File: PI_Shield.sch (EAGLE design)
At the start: 64 parts, among them J10 T2I, J11 T2I, J12 T2I, J13 DF13-4P-1.25DSA, J14 DF13-4P-1.25DSA, J15 DF13-4P-1.25DSA, J16 T2I5P, Q1 220mA/50V/3.5Ω, Q3 220mA/50V/3.5Ω, Q4 220mA/50V/3.5Ω, Q5 2.5A/30V/105mΩ, U1 MAX1136EUA-T, U2 AZ1117EH-3.3TRG1, Y1 ECS-80-S-4X

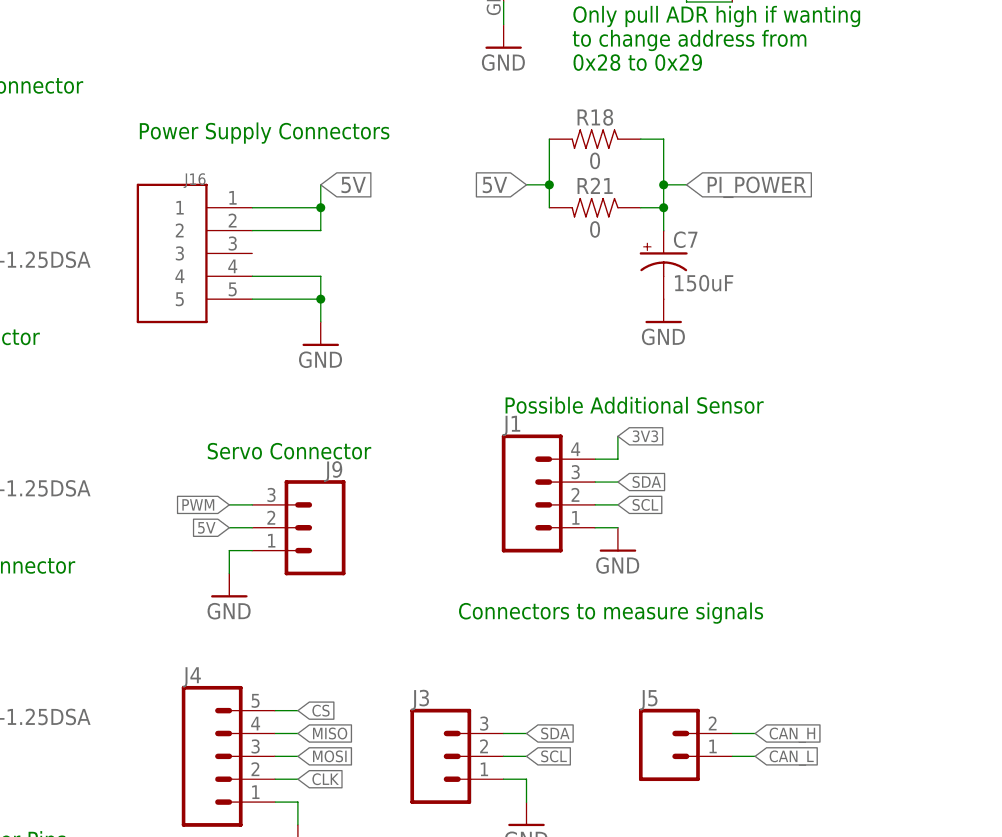
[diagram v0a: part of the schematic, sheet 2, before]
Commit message: add micro usb connector for external powering while testing
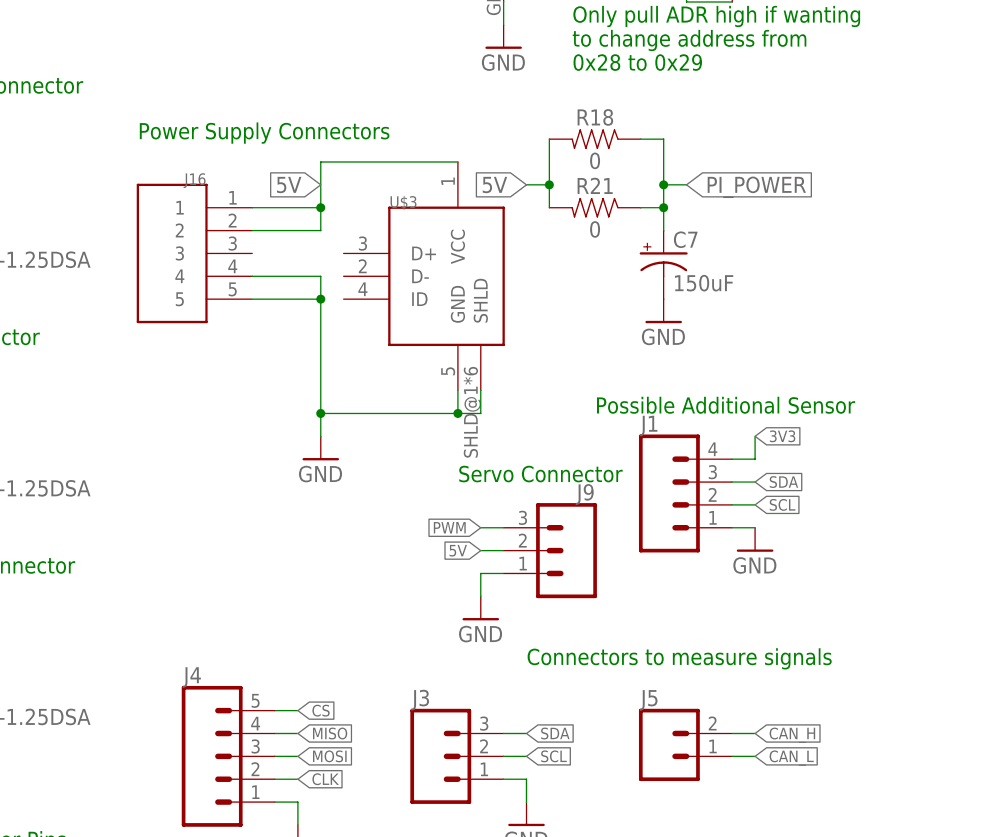
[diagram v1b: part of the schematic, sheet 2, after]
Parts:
- added U$3: USB-MICRO, usb conn:USB-MICRO
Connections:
- net 5V: now also U$3.VCC
- net GND: now also U$3.GND, U$3.SHLD
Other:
- moved on the sheet: J1, J9
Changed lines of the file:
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@@
 <part name="U$5" library="Adafruit IMUs - BNO055 and FX" deviceset="ADAFRUIT-BNO055" device=""/>
 <part name="GND31" library="supply1" library_urn="urn:adsk.eagle:library:371" deviceset="GND" device=""/>
+<part name="U$3" library="usb conn" deviceset="USB-MICRO" device=""/>
 </parts>
 <sheets>
@@
 <sheet>
 <plain>
-<text x="210.82" y="53.34" size="1.778" layer="91">Connectors to measure signals</text>
+<text x="218.44" y="48.26" size="1.778" layer="91">Connectors to measure signals</text>
 <text x="134.62" y="111.76" size="1.778" layer="91">Temperature Sensor Connector</text>
 <text x="134.62" y="83.82" size="1.778" layer="91">Pressure Sensor Connector</text>
@@
 <text x="193.04" y="160.02" size="1.778" layer="91">BNO055 IMU</text>
 <text x="175.26" y="106.68" size="1.778" layer="91">Power Supply Connectors</text>
-<text x="215.9" y="76.2" size="1.778" layer="91">Possible Additional Sensor</text>
+<text x="226.06" y="76.2" size="1.778" layer="91">Possible Additional Sensor</text>
 <text x="129.54" y="27.94" size="1.778" layer="91">UART Communication Header Pins</text>
-<text x="182.88" y="71.12" size="1.778" layer="91">Servo Connector</text>
+<text x="210.82" y="68.58" size="1.778" layer="91">Servo Connector</text>
 <text x="76.2" y="63.5" size="1.778" layer="91" rot="R90">We will be using Pi 4, not Pi 2</text>
 <text x="50.8" y="121.92" size="1.778" layer="91" rot="R180">DO NOT use pin 28 or 27
@@
 <attribute name="NAME" x="231.14" y="43.688" size="1.778" layer="95" font="vector"/>
 </instance>
-<instance part="GND3" gate="1" x="195.58" y="83.82" smashed="yes">
-<attribute name="VALUE" x="193.04" y="81.28" size="1.778" layer="96"/>
+<instance part="GND3" gate="1" x="195.58" y="71.12" smashed="yes">
+<attribute name="VALUE" x="193.04" y="68.58" size="1.778" layer="96"/>
 </instance>
 <instance part="C13" gate="G$1" x="238.76" y="152.4" smashed="yes">
@@
 <attribute name="VALUE" x="240.284" y="150.241" size="1.778" layer="96" font="vector"/>
 </instance>
-<instance part="J1" gate="G$1" x="220.98" y="66.04" smashed="yes">
-<attribute name="VALUE" x="215.9" y="58.674" size="1.778" layer="96" font="vector"/>
-<attribute name="NAME" x="215.9" y="74.168" size="1.778" layer="95" font="vector"/>
+<instance part="J1" gate="G$1" x="236.22" y="66.04" smashed="yes">
+<attribute name="VALUE" x="231.14" y="58.674" size="1.778" layer="96" font="vector"/>
+<attribute name="NAME" x="231.14" y="74.168" size="1.778" layer="95" font="vector"/>
 </instance>
 <instance part="J8" gate="J$1" x="134.62" y="17.78" smashed="yes">
@@
 <attribute name="VALUE" x="215.9" y="27.94" size="1.778" layer="96"/>
 </instance>
-<instance part="GND26" gate="1" x="228.6" y="60.96" smashed="yes">
-<attribute name="VALUE" x="226.06" y="58.42" size="1.778" layer="96"/>
+<instance part="GND26" gate="1" x="243.84" y="60.96" smashed="yes">
+<attribute name="VALUE" x="241.3" y="58.42" size="1.778" layer="96"/>
 </instance>
 <instance part="GND27" gate="1" x="215.9" y="116.84" smashed="yes">
@@
 <attribute name="VALUE" x="142.24" y="7.62" size="1.778" layer="96"/>
 </instance>
-<instance part="GND23" gate="1" x="185.42" y="55.88" smashed="yes">
-<attribute name="VALUE" x="182.88" y="53.34" size="1.778" layer="96"/>
+<instance part="GND23" gate="1" x="213.36" y="53.34" smashed="yes">
+<attribute name="VALUE" x="210.82" y="50.8" size="1.778" layer="96"/>
 </instance>
 <instance part="R18" gate="G$1" x="226.06" y="106.68" smashed="yes" rot="MR0">
@@
 <attribute name="NAME" x="182.88" y="101.6" size="1.27" layer="95" rot="MR0"/>
 </instance>
-<instance part="J9" gate="J$1" x="195.58" y="63.5" smashed="yes" rot="MR0">
-<attribute name="VALUE" x="198.12" y="56.134" size="1.778" layer="96" font="vector" rot="MR0"/>
-<attribute name="NAME" x="198.12" y="69.088" size="1.778" layer="95" font="vector" rot="MR0"/>
+<instance part="J9" gate="J$1" x="223.52" y="60.96" smashed="yes" rot="MR0">
+<attribute name="VALUE" x="226.06" y="53.594" size="1.778" layer="96" font="vector" rot="MR0"/>
+<attribute name="NAME" x="226.06" y="66.548" size="1.778" layer="95" font="vector" rot="MR0"/>
 </instance>
 <instance part="C7" gate="G$1" x="233.68" y="93.98" smashed="yes">
@@
 <instance part="GND31" gate="1" x="152.4" y="124.46" smashed="yes">
 <attribute name="VALUE" x="149.86" y="121.92" size="1.778" layer="96"/>
+</instance>
+<instance part="U$3" gate="G$1" x="205.74" y="96.52" smashed="yes">
+<attribute name="NAME" x="203.2" y="99.06" size="1.27" layer="95"/>
 </instance>
 </instances>
@@
 <wire x1="195.58" y1="91.44" x2="195.58" y2="88.9" width="0.1524" layer="91"/>
 <pinref part="GND3" gate="1" pin="GND"/>
-<wire x1="195.58" y1="88.9" x2="195.58" y2="86.36" width="0.1524" layer="91"/>
+<wire x1="195.58" y1="88.9" x2="195.58" y2="76.2" width="0.1524" layer="91"/>
 <junction x="195.58" y="88.9"/>
 <pinref part="J16" gate="&gt;NAME" pin="4"/>
 <pinref part="J16" gate="&gt;NAME" pin="5"/>
+<pinref part="U$3" gate="G$1" pin="SHLD"/>
+<wire x1="195.58" y1="76.2" x2="195.58" y2="73.66" width="0.1524" layer="91"/>
+<wire x1="213.36" y1="78.74" x2="213.36" y2="76.2" width="0.1524" layer="91"/>
+<wire x1="213.36" y1="76.2" x2="210.82" y2="76.2" width="0.1524" layer="91"/>
+<pinref part="U$3" gate="G$1" pin="GND"/>
+<wire x1="210.82" y1="76.2" x2="195.58" y2="76.2" width="0.1524" layer="91"/>
+<wire x1="210.82" y1="76.2" x2="210.82" y2="78.74" width="0.1524" layer="91"/>
+<junction x="210.82" y="76.2"/>
+<junction x="195.58" y="76.2"/>
 </segment>
 <segment>
 <pinref part="J1" gate="G$1" pin="1"/>
-<wire x1="226.06" y1="63.5" x2="228.6" y2="63.5" width="0.1524" layer="91"/>
+<wire x1="241.3" y1="63.5" x2="243.84" y2="63.5" width="0.1524" layer="91"/>
 <pinref part="GND26" gate="1" pin="GND"/>
 </segment>
@@
 </segment>
 <segment>
-<wire x1="187.96" y1="60.96" x2="185.42" y2="60.96" width="0.1524" layer="91"/>
+<wire x1="215.9" y1="58.42" x2="213.36" y2="58.42" width="0.1524" layer="91"/>
 <pinref part="GND23" gate="1" pin="GND"/>
-<wire x1="185.42" y1="60.96" x2="185.42" y2="58.42" width="0.1524" layer="91"/>
+<wire x1="213.36" y1="58.42" x2="213.36" y2="55.88" width="0.1524" layer="91"/>
 <pinref part="J9" gate="J$1" pin="1"/>
 </segment>
@@
 <segment>
 <pinref part="J1" gate="G$1" pin="3"/>
-<wire x1="226.06" y1="68.58" x2="228.6" y2="68.58" width="0.1524" layer="91"/>
-<label x="228.6" y="68.58" size="1.27" layer="95" xref="yes"/>
+<wire x1="241.3" y1="68.58" x2="243.84" y2="68.58" width="0.1524" layer="91"/>
+<label x="243.84" y="68.58" size="1.27" layer="95" xref="yes"/>
 </segment>
 <segment>
@@
 <segment>
 <pinref part="J1" gate="G$1" pin="2"/>
-<wire x1="226.06" y1="66.04" x2="228.6" y2="66.04" width="0.1524" layer="91"/>
-<label x="228.6" y="66.04" size="1.27" layer="95" xref="yes"/>
+<wire x1="241.3" y1="66.04" x2="243.84" y2="66.04" width="0.1524" layer="91"/>
+<label x="243.84" y="66.04" size="1.27" layer="95" xref="yes"/>
 </segment>
 <segment>
@@
 <net name="5V" class="2">
 <segment>
-<wire x1="187.96" y1="63.5" x2="185.42" y2="63.5" width="0.1524" layer="91"/>
+<wire x1="215.9" y1="60.96" x2="213.36" y2="60.96" width="0.1524" layer="91"/>
 <pinref part="J9" gate="J$1" pin="2"/>
-<label x="185.42" y="63.5" size="1.27" layer="95" rot="R180" xref="yes"/>
+<label x="213.36" y="60.96" size="1.27" layer="95" rot="R180" xref="yes"/>
 </segment>
 <segment>
@@
 <wire x1="187.96" y1="99.06" x2="195.58" y2="99.06" width="0.1524" layer="91"/>
 <wire x1="195.58" y1="96.52" x2="195.58" y2="99.06" width="0.1524" layer="91"/>
-<wire x1="195.58" y1="99.06" x2="195.58" y2="101.6" width="0.1524" layer="91"/>
 <junction x="195.58" y="99.06"/>
 <pinref part="J16" gate="&gt;NAME" pin="1"/>
 <pinref part="J16" gate="&gt;NAME" pin="2"/>
-<label x="195.58" y="101.6" size="1.778" layer="95" xref="yes"/>
+<label x="195.58" y="101.6" size="1.778" layer="95" rot="R180" xref="yes"/>
+<pinref part="U$3" gate="G$1" pin="VCC"/>
+<wire x1="210.82" y1="104.14" x2="195.58" y2="104.14" width="0.1524" layer="91"/>
+<wire x1="195.58" y1="104.14" x2="195.58" y2="99.06" width="0.1524" layer="91"/>
 </segment>
 </net>
@@
 <segment>
 <pinref part="J1" gate="G$1" pin="4"/>
-<wire x1="226.06" y1="71.12" x2="228.6" y2="71.12" width="0.1524" layer="91"/>
-<wire x1="228.6" y1="71.12" x2="228.6" y2="73.66" width="0.1524" layer="91"/>
-<label x="228.6" y="73.66" size="1.27" layer="95" xref="yes"/>
+<wire x1="241.3" y1="71.12" x2="243.84" y2="71.12" width="0.1524" layer="91"/>
+<wire x1="243.84" y1="71.12" x2="243.84" y2="73.66" width="0.1524" layer="91"/>
+<label x="243.84" y="73.66" size="1.27" layer="95" xref="yes"/>
 </segment>
 <segment>
@@
 <net name="PWM" class="0">
 <segment>
-<wire x1="187.96" y1="66.04" x2="185.42" y2="66.04" width="0.1524" layer="91"/>
+<wire x1="215.9" y1="63.5" x2="213.36" y2="63.5" width="0.1524" layer="91"/>
 <pinref part="J9" gate="J$1" pin="3"/>
-<label x="185.42" y="66.04" size="1.27" layer="95" rot="R180" xref="yes"/>
-</segment>
-<segment>
+<label x="213.36" y="63.5" size="1.27" layer="95" rot="R180" xref="yes"/>
+</segment>
+<segment>

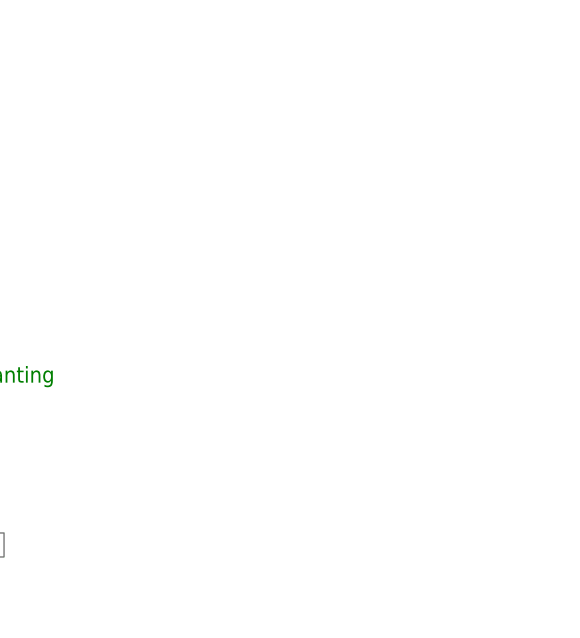
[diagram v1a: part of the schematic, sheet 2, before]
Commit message: update bno055 footprint
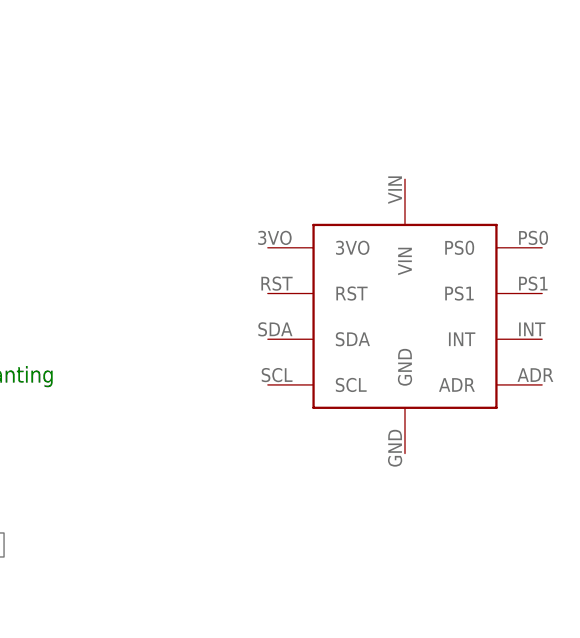
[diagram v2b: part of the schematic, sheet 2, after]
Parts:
- added U$6: BNO055_9DOF_BREAKOUT, Other:BNO055_9DOF_BREAKOUT
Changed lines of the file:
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@@
 <part name="GND31" library="supply1" library_urn="urn:adsk.eagle:library:371" deviceset="GND" device=""/>
 <part name="U$3" library="usb conn" deviceset="USB-MICRO" device=""/>
+<part name="U$6" library="Other" deviceset="BNO055_9DOF_BREAKOUT" device=""/>
 </parts>
 <sheets>
@@
 <attribute name="NAME" x="203.2" y="99.06" size="1.27" layer="95"/>
 </instance>
+<instance part="U$6" gate="G$1" x="297.18" y="124.46" smashed="yes"/>
 </instances>
 <busses>
